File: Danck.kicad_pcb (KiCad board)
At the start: 2 copper layers, 228.6 x 76.2 mm, 116 parts, among them SW1 SW_PUSH, U1 ProMicro

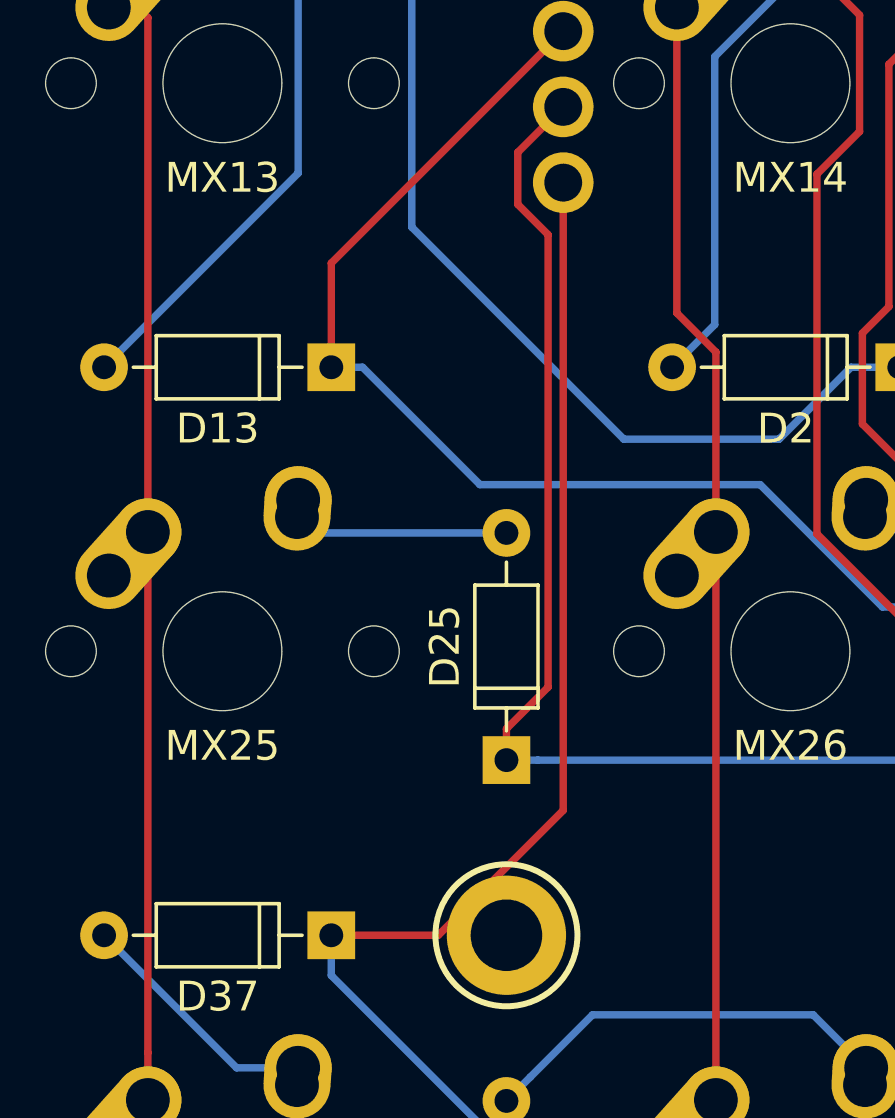
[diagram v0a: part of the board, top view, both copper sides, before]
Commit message: Fix DRC error, update gerbers
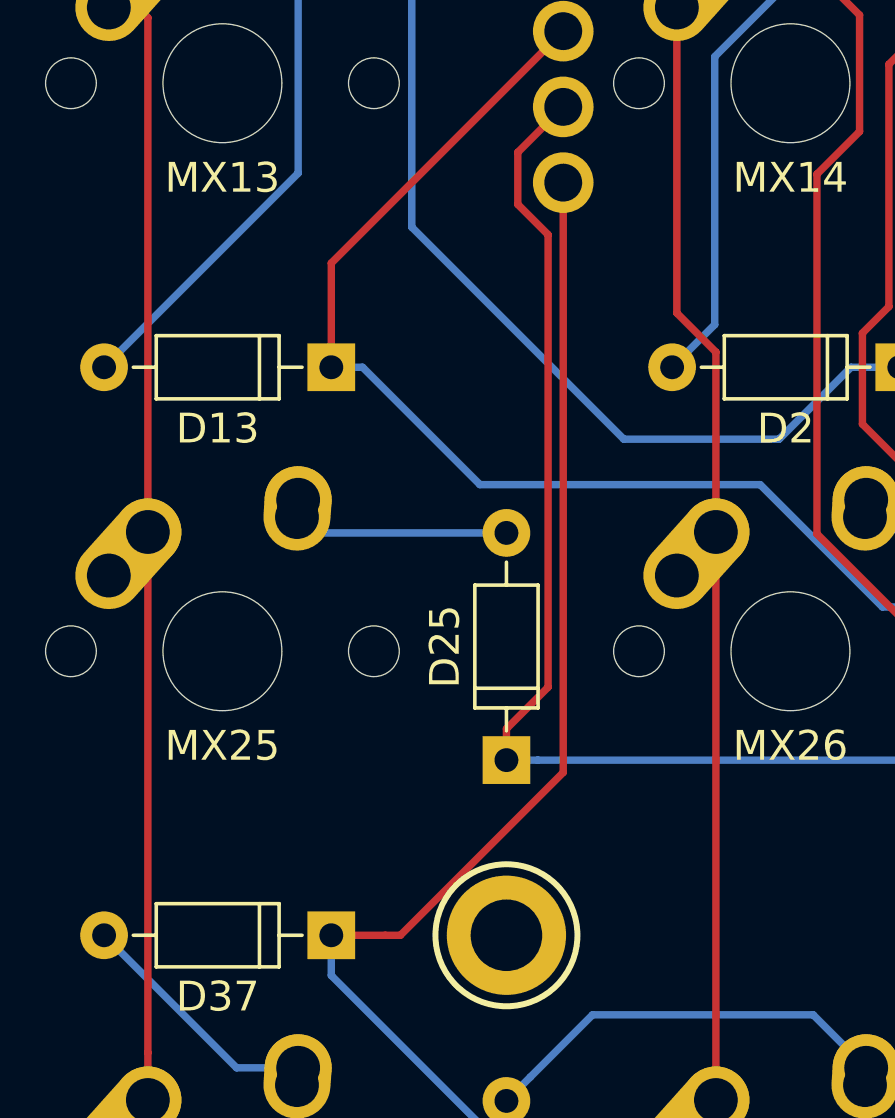
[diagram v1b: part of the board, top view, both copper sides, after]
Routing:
- net ROW3: track 261.1 -> 260.4 mm
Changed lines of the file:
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@@
     (links 248)
     (no_connects 0)
-    (area 17.470537 6.03125 283.28125 111.125001)
+    (area 8.818751 6.03125 283.28125 117.793751)
     (thickness 1.6)
     (drawings 34)
-    (tracks 428)
+    (tracks 429)
     (zones 0)
     (modules 116)
@@
   (segment (start 240.361249 69.995001) (end 238.924999 71.431251) (width 0.25) (layer B.Cu) (net 39))
   (segment (start 238.924999 71.431251) (end 238.125 72.23125) (width 0.25) (layer B.Cu) (net 39))
-  (segment (start 49.53 60.48375) (end 49.53 81.534) (width 0.25) (layer F.Cu) (net 40))
-  (segment (start 45.339 85.725) (end 41.75125 85.725) (width 0.25) (layer F.Cu) (net 40))
-  (segment (start 49.53 81.534) (end 45.339 85.725) (width 0.25) (layer F.Cu) (net 40))
+  (segment (start 49.53 60.48375) (end 49.53 80.264) (width 0.25) (layer F.Cu) (net 40))
+  (segment (start 49.53 80.264) (end 44.069 85.725) (width 0.25) (layer F.Cu) (net 40))
+  (segment (start 44.069 85.725) (end 43.561 85.725) (width 0.25) (layer F.Cu) (net 40))
+  (segment (start 43.561 85.725) (end 41.75125 85.725) (width 0.25) (layer F.Cu) (net 40))
   (segment (start 251.714 94.617974) (end 251.714 87.18775) (width 0.25) (layer B.Cu) (net 40))
   (segment (start 251.714 87.18775) (end 251.30125 86.775) (width 0.25) (layer B.Cu) (net 40))

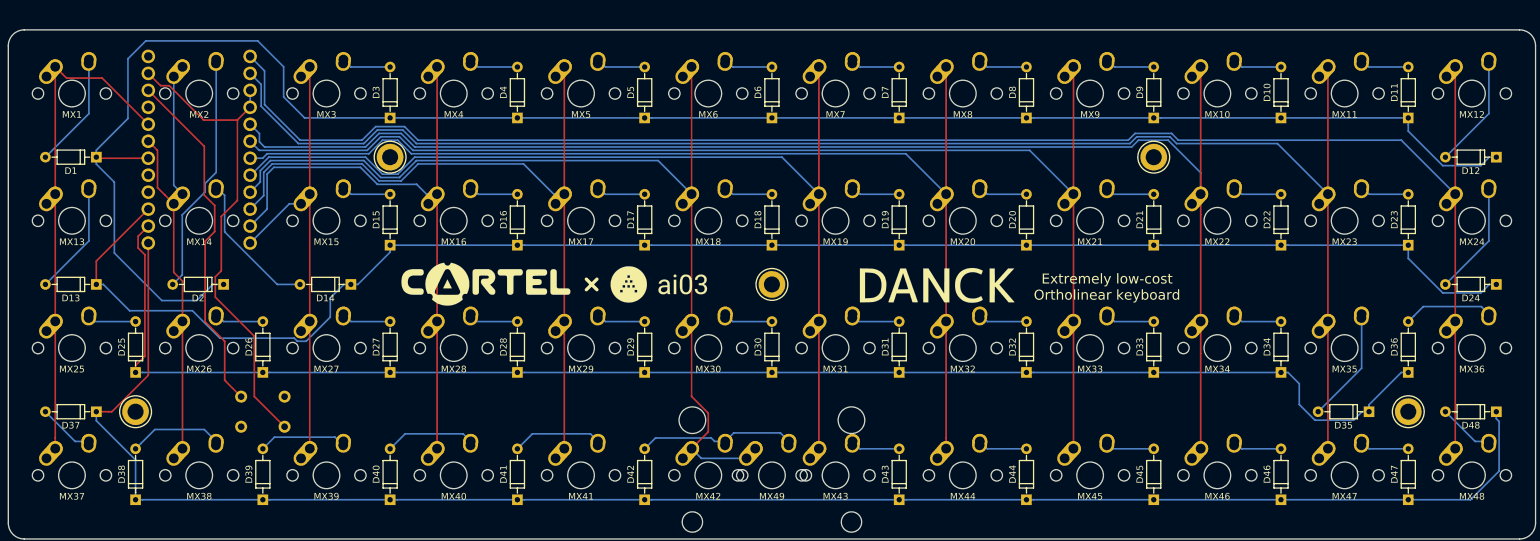
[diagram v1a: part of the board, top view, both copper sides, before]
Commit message: Unroute for moving pmicro
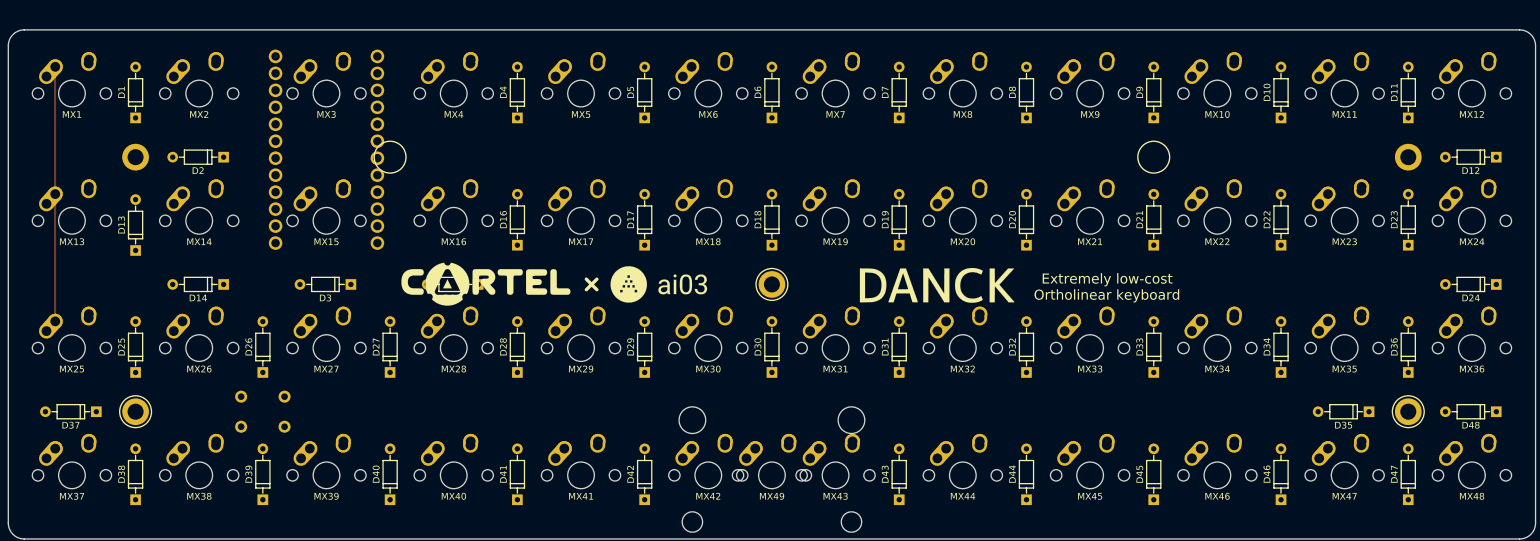
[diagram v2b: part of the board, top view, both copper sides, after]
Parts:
- moved G*** 88.9 mm to (-3.17, 46.0)
- moved REF** 38.1 mm to (238.1, 47.6)
- moved REF** 38.1 mm to (47.6, 47.6)
- moved D3 25.6 mm to (79.9, 66.7), turned to 180 degrees
- moved U1 19.1 mm to (76.2, 45.2)
- moved D2 19.0 mm to (60.8, 47.6)
- moved D14 19.0 mm to (60.8, 66.7)
- moved D15 14.4 mm to (98.9, 66.7), turned to 180 degrees
- moved D1 8.31 mm to (47.6, 41.8), turned to 90 degrees
- moved D13 7.77 mm to (47.6, 61.6), turned to 90 degrees
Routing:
- net ROW0: track 278.3 -> 0.00 mm
- net ROW3: track 260.4 -> 0.00 mm
- net COL11: track 251.5 -> 0.00 mm
- net ROW1: track 240.5 -> 0.00 mm
- net COL10: track 232.4 -> 0.00 mm
- net ROW2: track 222.4 -> 0.00 mm
- net COL9: track 208.9 -> 0.00 mm
- net COL8: track 185.3 -> 0.00 mm
- net COL7: track 165.8 -> 0.00 mm
- net COL6: track 147.8 -> 0.00 mm
- net COL5: track 142.9 -> 0.00 mm
- net COL4: track 114.6 -> 0.00 mm
- net COL3: track 93.5 -> 0.00 mm
- net GND: track 73.0 -> 0.00 mm
- net COL2: track 67.2 -> 0.00 mm
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
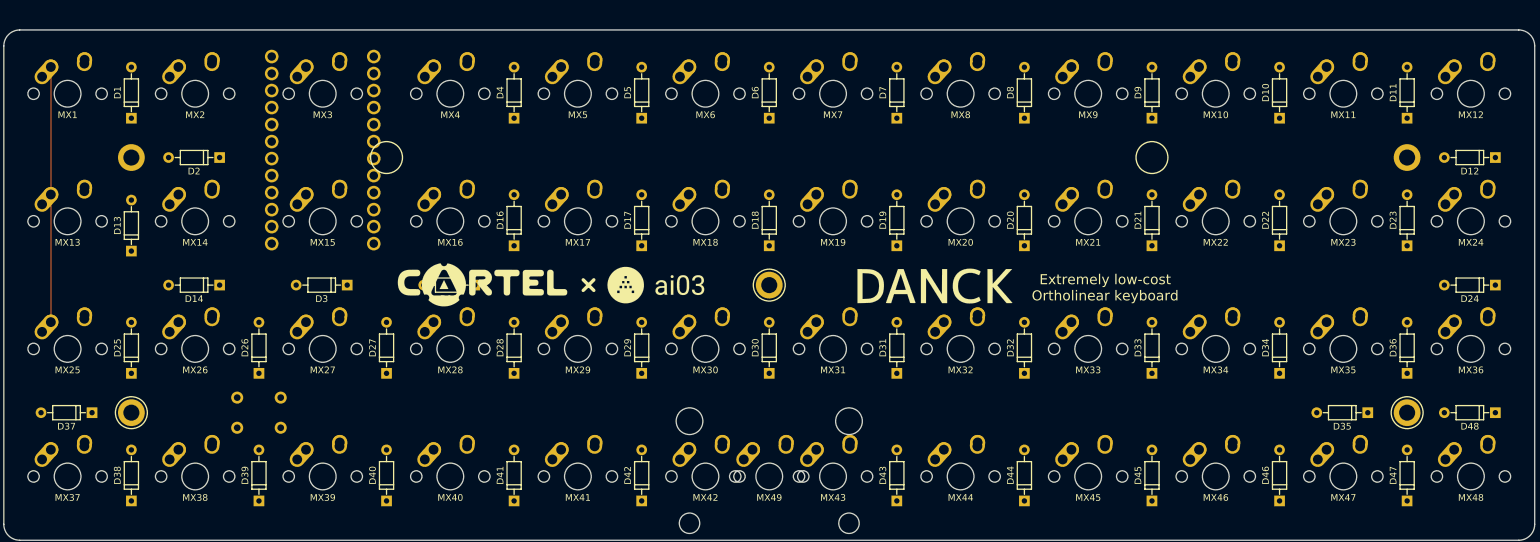
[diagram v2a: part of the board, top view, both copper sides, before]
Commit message: Finish reroute
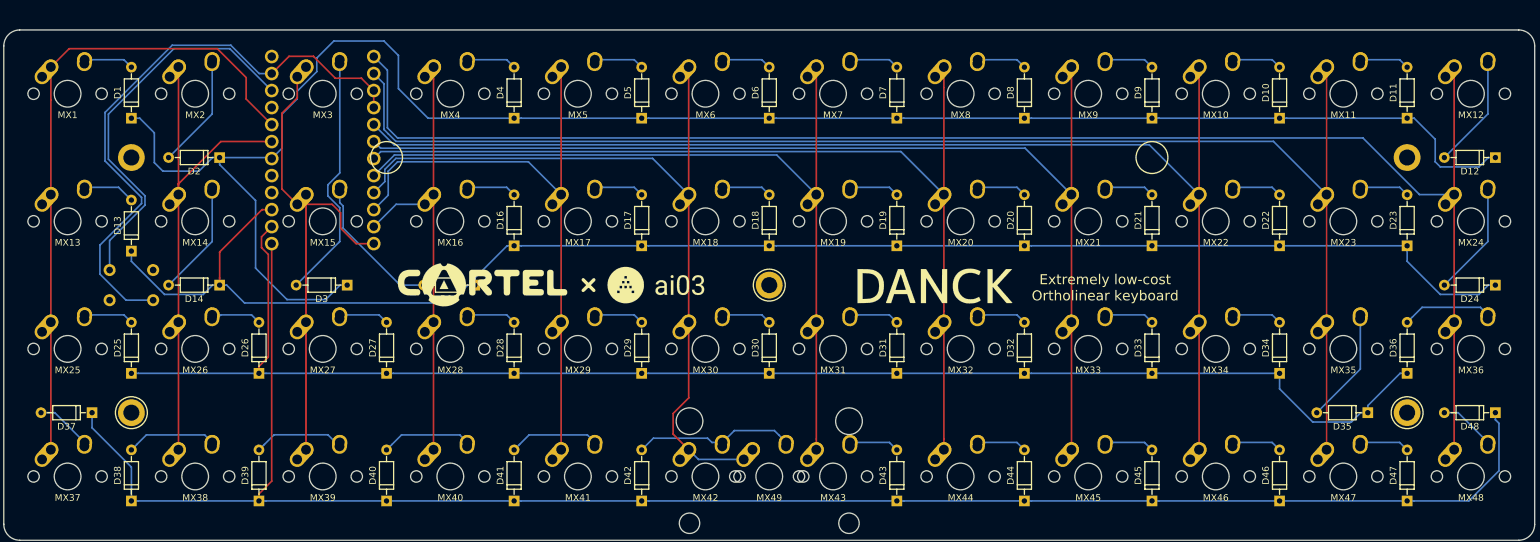
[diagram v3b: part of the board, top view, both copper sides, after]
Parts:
- moved SW1 26.9 mm to (47.6, 66.7)
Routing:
- net ROW0: track 0.00 -> 271.1 mm
- net ROW3: track 0.00 -> 269.8 mm
- net ROW1: track 0.00 -> 233.4 mm
- net COL11: track 0.00 -> 232.1 mm
- net ROW2: track 0.00 -> 222.0 mm
- net COL10: track 0.00 -> 212.9 mm
- net COL9: track 0.00 -> 184.7 mm
- net COL8: track 0.00 -> 164.6 mm
- net COL7: track 0.00 -> 145.4 mm
- net COL6: track 0.00 -> 127.0 mm
- net COL5: track 0.00 -> 120.3 mm
- net COL4: track 0.00 -> 93.9 mm
- net GND: track 0.00 -> 90.3 mm
- net COL1: track 0.00 -> 75.3 mm
- net COL2: track 0.00 -> 74.2 mm
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
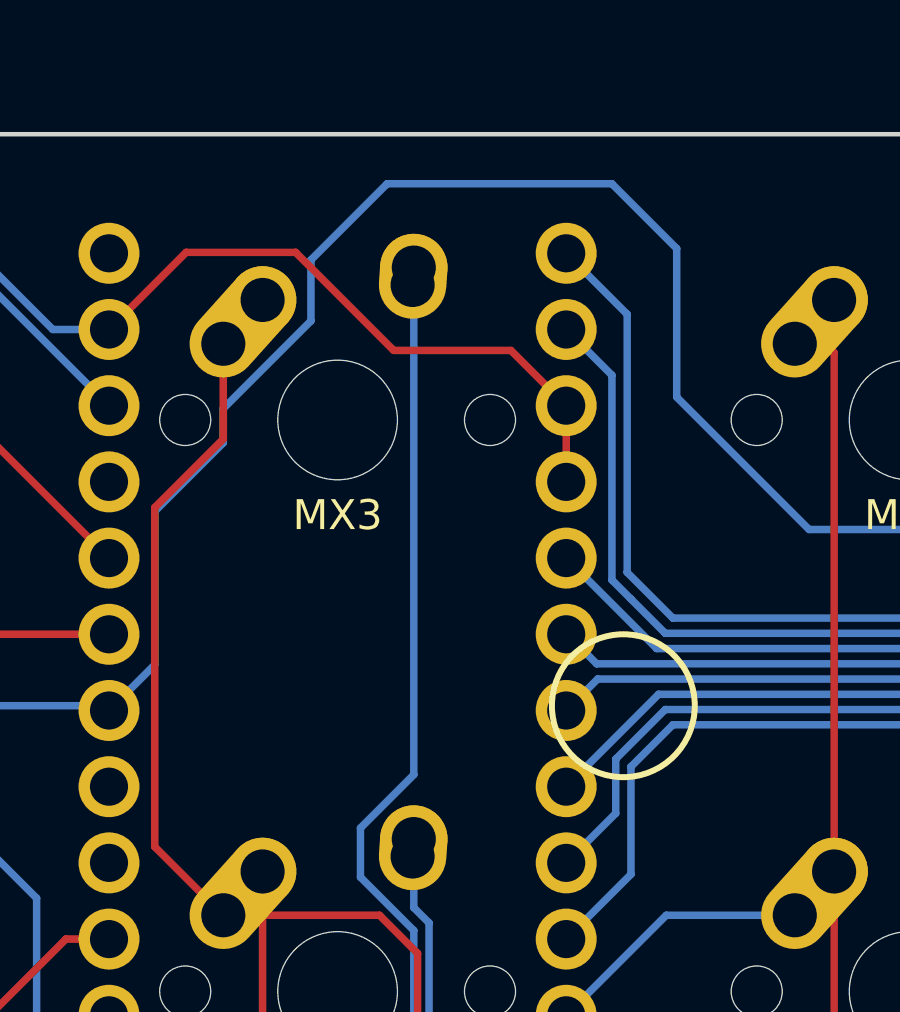
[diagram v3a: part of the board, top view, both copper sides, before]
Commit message: Make gnd plane flow better
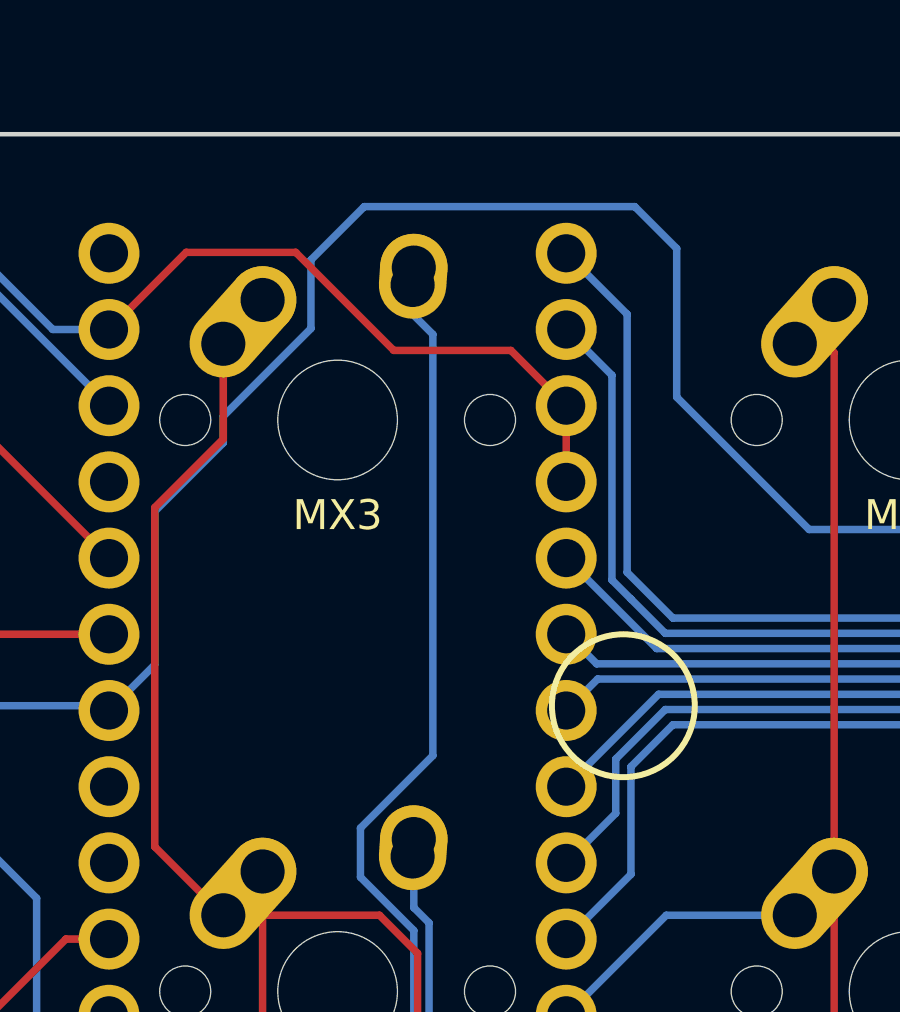
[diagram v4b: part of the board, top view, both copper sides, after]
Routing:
- net ROW0: track 271.1 -> 270.5 mm
- net Net-(D3-Pad2): track 37.8 -> 38.4 mm
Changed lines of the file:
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@@
   (general
     (links 248)
-    (no_connects 147)
-    (area 8.818751 6.03125 283.28125 117.793751)
+    (no_connects 0)
+    (area -12.92399 6.03125 283.28125 117.793751)
     (thickness 1.6)
     (drawings 34)
-    (tracks 410)
+    (tracks 412)
     (zones 0)
     (modules 116)
@@
   (segment (start 104.775 41.75125) (end 91.91625 41.75125) (width 0.25) (layer B.Cu) (net 1))
   (segment (start 91.91625 41.75125) (end 87.503 37.338) (width 0.25) (layer B.Cu) (net 1))
-  (segment (start 72.39 37.719) (end 72.39 38.862) (width 0.25) (layer B.Cu) (net 1))
-  (segment (start 72.39 38.862) (end 70.104 41.148) (width 0.25) (layer B.Cu) (net 1))
+  (segment (start 72.39 37.973) (end 72.39 38.862) (width 0.25) (layer B.Cu) (net 1))
   (segment (start 87.503 37.338) (end 87.503 32.385) (width 0.25) (layer B.Cu) (net 1))
-  (segment (start 87.503 32.385) (end 85.344 30.226) (width 0.25) (layer B.Cu) (net 1))
-  (segment (start 85.344 30.226) (end 77.851 30.226) (width 0.25) (layer B.Cu) (net 1))
-  (segment (start 77.851 30.226) (end 75.311 32.766) (width 0.25) (layer B.Cu) (net 1))
+  (segment (start 87.503 32.385) (end 86.106 30.988) (width 0.25) (layer B.Cu) (net 1))
+  (segment (start 86.106 30.988) (end 77.089 30.988) (width 0.25) (layer B.Cu) (net 1))
+  (segment (start 75.311 32.766) (end 75.311 35.052) (width 0.25) (layer B.Cu) (net 1))
+  (segment (start 77.089 30.988) (end 75.311 32.766) (width 0.25) (layer B.Cu) (net 1))
+  (segment (start 75.311 35.052) (end 72.39 37.973) (width 0.25) (layer B.Cu) (net 1))
+  (segment (start 72.39 38.862) (end 70.104 41.148) (width 0.25) (layer B.Cu) (net 1))
   (segment (start 70.104 41.148) (end 70.104 46.25975) (width 0.25) (layer B.Cu) (net 1))
-  (segment (start 75.311 32.766) (end 75.311 34.798) (width 0.25) (layer B.Cu) (net 1))
-  (segment (start 75.311 34.798) (end 72.39 37.719) (width 0.25) (layer B.Cu) (net 1))
   (segment (start 70.104 46.25975) (end 68.58 47.78375) (width 0.25) (layer B.Cu) (net 1))
   (segment (start 47.625 41.75125) (end 48.86325 41.75125) (width 0.25) (layer B.Cu) (net 1))
@@
   (segment (start 59.69 33.02) (end 59.69 41.11625) (width 0.25) (layer B.Cu) (net 3))
   (segment (start 59.69 41.11625) (end 53.18125 47.625) (width 0.25) (layer B.Cu) (net 3))
-  (segment (start 78.74 33.02) (end 78.74 49.923998) (width 0.25) (layer B.Cu) (net 4))
-  (segment (start 78.74 49.923998) (end 76.962 51.701998) (width 0.25) (layer B.Cu) (net 4))
-  (segment (start 76.962 53.34) (end 78.74 55.118) (width 0.25) (layer B.Cu) (net 4))
-  (segment (start 76.962 51.701998) (end 76.962 53.34) (width 0.25) (layer B.Cu) (net 4))
+  (segment (start 78.74 33.02) (end 78.74 34.61099) (width 0.25) (layer B.Cu) (net 4))
+  (segment (start 78.74 34.61099) (end 79.375 35.24599) (width 0.25) (layer B.Cu) (net 4))
+  (segment (start 79.375 35.24599) (end 79.375 49.288998) (width 0.25) (layer B.Cu) (net 4))
+  (segment (start 79.375 49.288998) (end 76.962 51.701998) (width 0.25) (layer B.Cu) (net 4))
   (segment (start 78.74 55.118) (end 78.74 60.16625) (width 0.25) (layer B.Cu) (net 4))
+  (segment (start 76.962 51.701998) (end 76.962 53.34) (width 0.25) (layer B.Cu) (net 4))
+  (segment (start 76.962 53.34) (end 78.74 55.118) (width 0.25) (layer B.Cu) (net 4))
   (segment (start 78.74 60.16625) (end 78.613 60.29325) (width 0.25) (layer B.Cu) (net 4))
   (segment (start 78.613 60.29325) (end 72.23125 66.675) (width 0.25) (layer B.Cu) (net 4))

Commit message: Update some memes
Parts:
- removed the G*** at (156.4, 69.5)
- removed the G*** at (77.0, 88.1)
- added G***: LOGO, memelogo:thonksmall, B.Cu at (72.3, 84.7)
- added G***: LOGO, memelogo:boboxsmall, B.Cu at (146.8, 77.9)
- added G***: LOGO, memelogo:righthand, B.Cu at (179.5, 65.5)
- added G***: LOGO, memelogo:stem, B.Cu at (91.2, 46.1)
- moved G*** 46.4 mm to (43.2, 46.6)
- moved G*** 40.7 mm to (180.7, 83.4)
- moved G*** 37.5 mm to (218.4, 84.7)
- moved G*** 12.3 mm to (46.0, 86.2)
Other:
- board text added: "Pro Micro here! Component side faces away from the PCB. Rev 1.1"

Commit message: breakout pins
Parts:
- added P1: Pad, locallib:mountinghole, F.Cu at (35.7, 66.7)
- added P2: Pad, locallib:mountinghole, F.Cu at (38.2, 66.7)
- added P3: Pad, locallib:mountinghole, F.Cu at (33.1, 66.7)
- added P4: Pad, locallib:mountinghole, F.Cu at (40.8, 66.7)
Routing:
- net +5V: track 0.00 -> 77.3 mm, vias 0 -> 1
- net Net-(P1-Pad1): track 0.00 -> 48.4 mm, vias 0 -> 1
- net Net-(P2-Pad1): track 0.00 -> 42.7 mm, vias 0 -> 1
- net COL0: track 97.8 -> 105.3 mm
- net GND: track 90.3 -> 93.6 mm
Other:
- board text added: "5V 17 16 GND"
- board text added: "Pro Micro here! Component side faces away from the PCB. Rev 1.2"
- board text removed: "Pro Micro here! Component side faces away from the PCB. Rev 1.1"

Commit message: REEEEEE
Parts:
- added G***: LOGO, memelogo:reeeeeee, B.Cu at (221.5, 47.6)
- moved G*** 7.12 mm to (172.3, 65.8)
